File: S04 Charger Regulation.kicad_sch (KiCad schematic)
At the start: 24 parts, among them Q6 DMT4011LFG, Q7 DMT4011LFG, U1 LTC1960

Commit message: Add D5: DNP alternate for D2 at its original 0.5.0 position
- S04: D5 (SS0540, SOD-123) in parallel with D2 on the charger switch
  node and GND, marked DNP, with a NOTE explaining it is an alternate
  to D2.
- PCB: D5 placed where D2 sat on the Altium 0.5.0 board (pads at
  195.70/126.27 and 195.70/129.54, rotated 270). The Net-(D2-C) F.Cu
  pour gets a small tab to reach the D5 cathode; the anode is in the
  GND pour. Zones refilled.
- The board diff is mostly KiCad re-sorting the FET paste-window pads
  on save; no other geometry changed.

ERC 0. DRC: 0 unconnected, 0 parity; remaining items unchanged
(excluded layer-marker edge clearances, silk overlap, text thickness).

Co-Authored-By: Claude Opus 5.5 <noreply@anthropic.com>
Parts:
- added D5: SS0540 40V, EVO2513-0_5_0-import-fps:Diode SOD123, symbol Lattech Systems:Diode Schottky SS0540 0.5A SOD-123
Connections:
- net GND: now also D5.2 (A)
- net at C16.2, D2.1 (C), L1.1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: now also D5.1 (C)

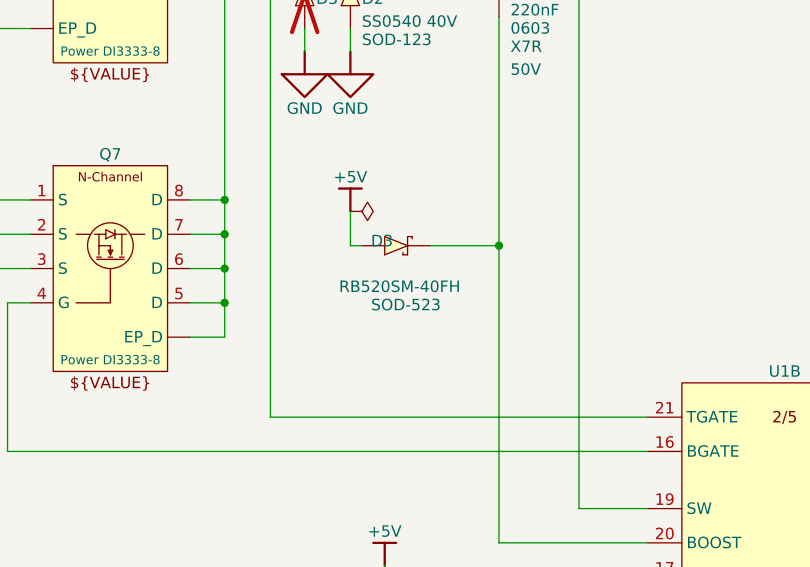
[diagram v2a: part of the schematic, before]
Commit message: D3: KiCad D_SOD-523 footprint, Rohm manufacturer and reel part number
- D3 (RB520SM-40FH) moves from the imported "Diode SOD523" footprint to
  Diode_SMD:D_SOD-523 with the KiCad 3D model; embedded SOD523.STEP dropped.
- MANUFACTURER: On Semiconductor -> Rohm Semiconductor.
- MANUFACTURER_PN: RB520SM-40FH -> RB520SM-40FHT2R (tape and reel).

Co-Authored-By: Claude Opus 5.5 <noreply@anthropic.com>
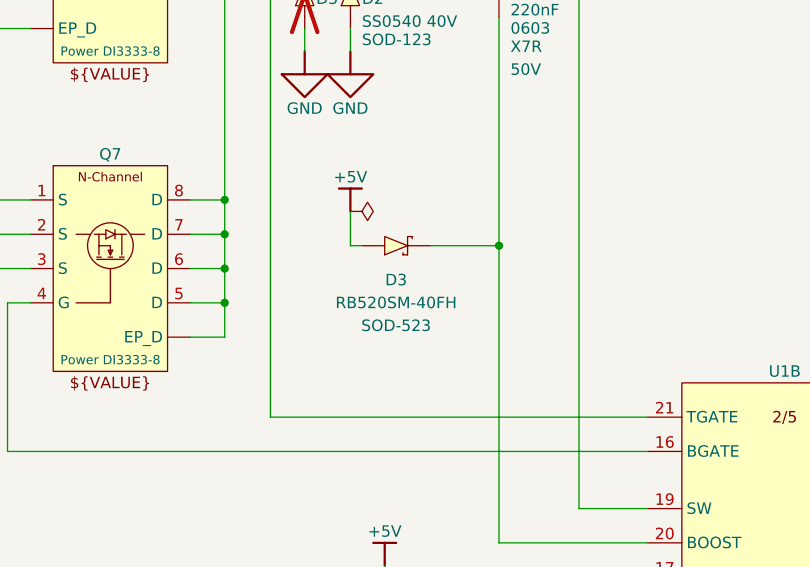
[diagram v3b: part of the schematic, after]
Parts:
- D3: footprint EVO2513-0_5_0-import-fps:Diode SOD523 -> Diode_SMD:D_SOD-523; MANUFACTURER On Semiconductor -> Rohm Semiconductor; MANUFACTURER_PN RB520SM-40FH -> RB520SM-40FHT2R
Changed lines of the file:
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@@
 		(in_pos_files yes)
 		(dnp no)
+		(fields_autoplaced yes)
 		(property "Reference" "D3"
-			(at 145.796 125.73 0)
+			(at 148.59 130.81 0)
 			(show_name no)
 			(do_not_autoplace no)
@@
 					(size 1.27 1.27)
 				)
-				(justify left bottom)
 			)
 		)
@@
 			)
 		)
-		(property "Footprint" "EVO2513-0_5_0-import-fps:Diode SOD523"
+		(property "Footprint" "Diode_SMD:D_SOD-523"
 			(at 148.59 127 0)
 			(hide yes)
@@
 			)
 		)
-		(property "MANUFACTURER" "On Semiconductor"
+		(property "MANUFACTURER" "Rohm Semiconductor"
 			(at 144.272 125.73 0)
 			(hide yes)
@@
 			)
 		)
-		(property "MANUFACTURER_PN" "RB520SM-40FH"
+		(property "MANUFACTURER_PN" "RB520SM-40FHT2R"
 			(at 144.272 125.73 0)
 			(hide yes)
@@
 		)
 		(property "ALTIUM_VALUE" "RB520SM-40FH"
-			(at 142.24 130.81 0)
+			(at 148.59 133.35 0)
 			(show_name no)
 			(do_not_autoplace no)
@@
 					(size 1.27 1.27)
 				)
-				(justify left bottom)
 			)
 		)
 		(property "ALTIUM_FOOTPRINT" "SOD-523"
-			(at 145.796 132.842 0)
+			(at 148.59 135.89 0)
 			(show_name no)
 			(do_not_autoplace no)
@@
 					(size 1.27 1.27)
 				)
-				(justify left bottom)
 			)
 		)

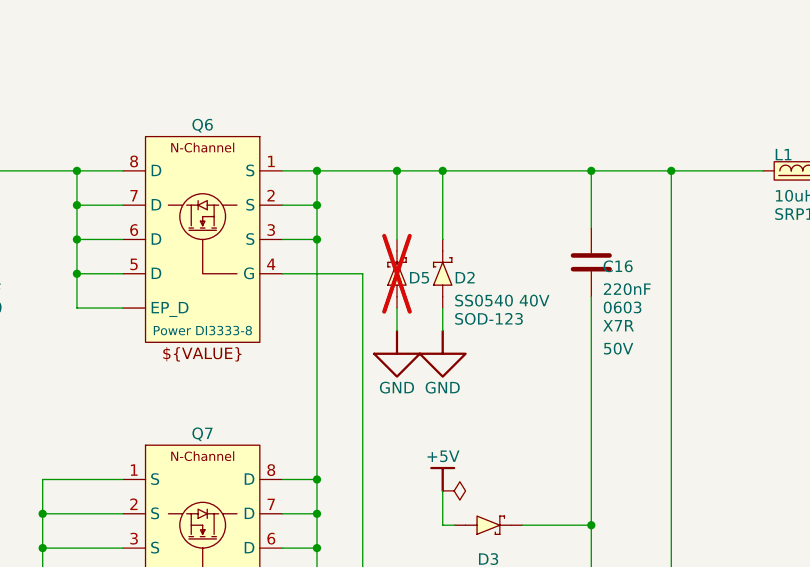
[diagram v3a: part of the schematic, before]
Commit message: Remove D5, the DNP alternate for D2
D2's position and the SW routing are settled, so the optional D5 is
dropped from the schematic, the board and the README. Its GND symbol,
stub wires and junction go with it.

Co-Authored-By: Claude Opus 5.5 <noreply@anthropic.com>
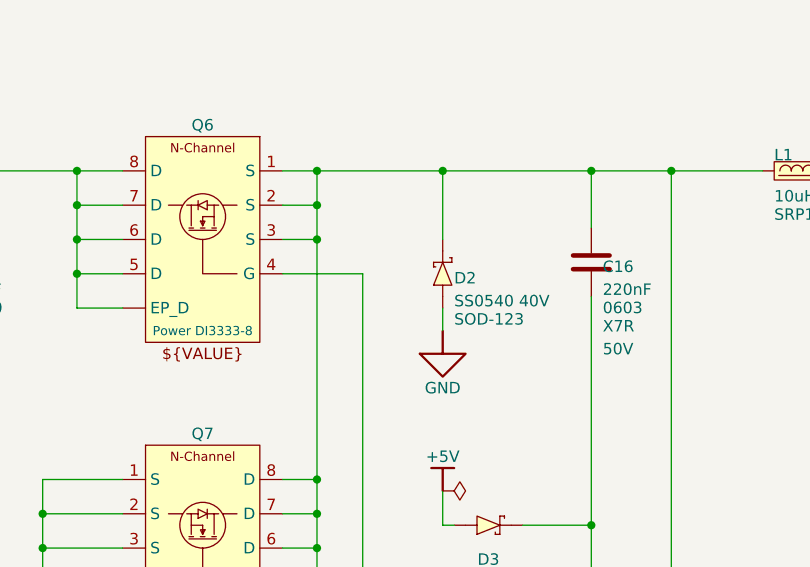
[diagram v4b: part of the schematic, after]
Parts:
- removed D5: SS0540 40V, EVO2513-0_5_0-import-fps:Diode SOD123, symbol Lattech Systems:Diode Schottky SS0540 0.5A SOD-123

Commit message: D2: KiCad D_SOD-123 footprint
D2 (Panjit SS0540) moves from the imported "Diode SOD123" footprint to
Diode_SMD:D_SOD-123 with the KiCad 3D model; pads are within 0.07 mm of
Panjit's land pattern. Embedded STEP dropped from the footprint.

Co-Authored-By: Claude Opus 5.5 <noreply@anthropic.com>
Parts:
- D2: footprint EVO2513-0_5_0-import-fps:Diode SOD123 -> Diode_SMD:D_SOD-123
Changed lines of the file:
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@@
 			)
 		)
-		(property "Footprint" "EVO2513-0_5_0-import-fps:Diode SOD123"
+		(property "Footprint" "Diode_SMD:D_SOD-123"
 			(at 143.51 99.06 0)
 			(hide yes)

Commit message: Fill manufacturer part numbers from the 0.5.0 build orders
Set MANUFACTURER and MANUFACTURER_PN on every fitted part, in the
schematic and on the board. Unchanged parts take the exact part numbers
ordered for the 0.5.0 backup build (DigiKey list and Mouser basket);
changed parts reuse an ordered part where value, package and rating
match; the rest keep the schematic's part or take a Yageo RC/CC part.

Co-Authored-By: Claude Opus 5.5 <noreply@anthropic.com>
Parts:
- C13, C14, C24, C25, C26: MANUFACTURER Murata -> Murata Electronics
- C15: MANUFACTURER (none) -> Murata Electronics; MANUFACTURER_PN (none) -> GRM219R61A475KE34J
- C16, C22: MANUFACTURER Yageo -> YAGEO; MANUFACTURER_PN CC0603KRX7R9BB224 -> AC0603KRX7R9BB224
- C17, C18, C20, C21: MANUFACTURER Yageo -> YAGEO
- C19: MANUFACTURER ? -> YAGEO; MANUFACTURER_PN ? -> CC0402JRNPO9BN101
- C23: MANUFACTURER ? -> Samsung Electro-Mechanics; MANUFACTURER_PN ? -> CL10A105KB8NNNC
- D2: MANUFACTURER Panjit -> Panjit International Inc.; MANUFACTURER_PN SS0540 -> SS0540_R1_00001
- L1: MANUFACTURER Bourns -> Bourns Inc.
- Q6, Q7: MANUFACTURER Diodes Inc -> Diodes Incorporated; MANUFACTURER_PN DMT4011LFG -> DMT4011LFG-13
- R19: MANUFACTURER (none) -> Bourns Inc.
- R20: MANUFACTURER (none) -> YAGEO; MANUFACTURER_PN (none) -> RC0402FR-073K6L
- R21: MANUFACTURER ? -> YAGEO; MANUFACTURER_PN ? -> RC0402FR-07100RL
- U1: MANUFACTURER Analog Devices -> Analog Devices Inc.; MANUFACTURER_PN LTC1960CUHF -> LTC1960CUHF#PBF
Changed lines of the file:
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@@
 			)
 		)
-		(property "MANUFACTURER" "?"
+		(property "MANUFACTURER" "YAGEO"
 			(at 220.98 176.022 0)
 			(hide yes)
@@
 			)
 		)
-		(property "MANUFACTURER_PN" "?"
+		(property "MANUFACTURER_PN" "CC0402JRNPO9BN101"
 			(at 220.98 176.022 0)
 			(hide yes)
@@
 			)
 		)
-		(property "MANUFACTURER" "?"
+		(property "MANUFACTURER" "YAGEO"
 			(at 246.634 127.762 0)
 			(hide yes)
@@
 			)
 		)
-		(property "MANUFACTURER_PN" "?"
+		(property "MANUFACTURER_PN" "RC0402FR-07100RL"
 			(at 246.634 127.762 0)
 			(hide yes)
@@
 			)
 		)
-		(property "MANUFACTURER" ""
+		(property "MANUFACTURER" "Murata Electronics"
 			(at 148.59 168.402 0)
 			(hide yes)
@@
 			)
 		)
-		(property "MANUFACTURER_PN" ""
+		(property "MANUFACTURER_PN" "GRM219R61A475KE34J"
 			(at 148.59 168.402 0)
 			(hide yes)
@@
 			)
 		)
-		(property "MANUFACTURER" "Diodes Inc"
+		(property "MANUFACTURER" "Diodes Incorporated"
 			(at 125.222 81.28 0)
 			(hide yes)
@@
 			)
 		)
-		(property "MANUFACTURER_PN" "DMT4011LFG"
+		(property "MANUFACTURER_PN" "DMT4011LFG-13"
 			(at 125.222 81.28 0)
 			(hide yes)
@@
 			)
 		)
-		(property "MANUFACTURER" "Bourns"
+		(property "MANUFACTURER" "Bourns Inc."
 			(at 178.562 86.614 0)
 			(hide yes)
@@
 			)
 		)
-		(property "MANUFACTURER" "Murata"
+		(property "MANUFACTURER" "Murata Electronics"
 			(at 295.91 94.742 0)
 			(hide yes)
@@
 			)
 		)
-		(property "MANUFACTURER" "Murata"
+		(property "MANUFACTURER" "Murata Electronics"
 			(at 76.2 93.472 0)
 			(hide yes)
@@
 			)
 		)
-		(property "MANUFACTURER" "?"
+		(property "MANUFACTURER" "Samsung Electro-Mechanics"
 			(at 269.24 94.742 0)
 			(hide yes)
@@
 			)
 		)
-		(property "MANUFACTURER_PN" "?"
+		(property "MANUFACTURER_PN" "CL10A105KB8NNNC"
 			(at 269.24 94.742 0)
 			(hide yes)
@@
 			)
 		)
-		(property "MANUFACTURER" "Yageo"
+		(property "MANUFACTURER" "YAGEO"
 			(at 246.38 140.462 0)
 			(hide yes)
@@
 			)
 		)
-		(property "MANUFACTURER" "Diodes Inc"
+		(property "MANUFACTURER" "Diodes Incorporated"
 			(at 107.442 115.57 0)
 			(hide yes)
@@
 			)
 		)
-		(property "MANUFACTURER_PN" "DMT4011LFG"
+		(property "MANUFACTURER_PN" "DMT4011LFG-13"
 			(at 107.442 115.57 0)
 			(hide yes)
@@
 			)
 		)
-		(property "MANUFACTURER" "Murata"
+		(property "MANUFACTURER" "Murata Electronics"
 			(at 283.21 94.742 0)
 			(hide yes)
@@
 			)
 		)
-		(property "MANUFACTURER" ""
+		(property "MANUFACTURER" "YAGEO"
 			(at 231.394 165.862 0)
 			(hide yes)
@@
 			)
 		)
-		(property "MANUFACTURER_PN" ""
+		(property "MANUFACTURER_PN" "RC0402FR-073K6L"
 			(at 231.394 165.862 0)
 			(hide yes)
@@
 			)
 		)
-		(property "MANUFACTURER" "Analog Devices"
+		(property "MANUFACTURER" "Analog Devices Inc."
 			(at 176.022 142.24 0)
 			(hide yes)
@@
 			)
 		)
-		(property "MANUFACTURER_PN" "LTC1960CUHF"
+		(property "MANUFACTURER_PN" "LTC1960CUHF#PBF"
 			(at 176.022 142.24 0)
 			(hide yes)
@@
 			)
 		)
-		(property "MANUFACTURER" ""
+		(property "MANUFACTURER" "Bourns Inc."
 			(at 225.552 83.82 90)
 			(hide yes)
@@
 			)
 		)
-		(property "MANUFACTURER" "Murata"
+		(property "MANUFACTURER" "Murata Electronics"
 			(at 308.61 94.742 0)
 			(hide yes)
@@
 			)
 		)
-		(property "MANUFACTURER" "Yageo"
+		(property "MANUFACTURER" "YAGEO"
 			(at 246.38 176.022 0)
 			(hide yes)
@@
 			)
 		)
-		(property "MANUFACTURER_PN" "CC0603KRX7R9BB224"
+		(property "MANUFACTURER_PN" "AC0603KRX7R9BB224"
 			(at 246.38 176.022 0)
 			(hide yes)
@@
 			)
 		)
-		(property "MANUFACTURER" "Yageo"
+		(property "MANUFACTURER" "YAGEO"
 			(at 158.75 168.402 0)
 			(hide yes)
@@
 			)
 		)
-		(property "MANUFACTURER" "Panjit"
+		(property "MANUFACTURER" "Panjit International Inc."
 			(at 142.24 94.742 90)
 			(hide yes)
@@
 			)
 		)
-		(property "MANUFACTURER_PN" "SS0540"
+		(property "MANUFACTURER_PN" "SS0540_R1_00001"
 			(at 142.24 94.742 90)
 			(hide yes)
@@
 			)
 		)
-		(property "MANUFACTURER" "Yageo"
+		(property "MANUFACTURER" "YAGEO"
 			(at 158.75 93.472 0)
 			(hide yes)
@@
 			)
 		)
-		(property "MANUFACTURER_PN" "CC0603KRX7R9BB224"
+		(property "MANUFACTURER_PN" "AC0603KRX7R9BB224"
 			(at 158.75 93.472 0)
 			(hide yes)
@@
 			)
 		)
-		(property "MANUFACTURER" "Murata"
+		(property "MANUFACTURER" "Murata Electronics"
 			(at 87.63 93.472 0)
 			(hide yes)
@@
 			)
 		)
-		(property "MANUFACTURER" "Yageo"
+		(property "MANUFACTURER" "YAGEO"
 			(at 231.14 176.022 0)
 			(hide yes)
@@
 			)
 		)
-		(property "MANUFACTURER" "Yageo"
+		(property "MANUFACTURER" "YAGEO"
 			(at 210.82 176.022 0)
 			(hide yes)

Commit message: Move capacitors to currently available part numbers
C32 to Murata GRM219R61C226ME15L (GRM21BR61C226ME44L is no longer
generally available), C39 to Yageo CC0805KPX7R9BB102, the 1 uF 0603
caps to Murata GRT188R61H105KE13D, and the 10 uF 1210 caps to Taiyo
Yuden UMK325AB7106KMHP.

Co-Authored-By: Claude Opus 5.5 <noreply@anthropic.com>
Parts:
- C13, C14, C24, C25, C26: MANUFACTURER Murata Electronics -> Taiyo Yuden; MANUFACTURER_PN GRM32ER71H106KA12L -> UMK325AB7106KMHP
- C23: MANUFACTURER Samsung Electro-Mechanics -> Murata Electronics; MANUFACTURER_PN CL10A105KB8NNNC -> GRT188R61H105KE13D
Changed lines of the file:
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@@
 			)
 		)
-		(property "MANUFACTURER" "Murata Electronics"
+		(property "MANUFACTURER" "Taiyo Yuden"
 			(at 295.91 94.742 0)
 			(hide yes)
@@
 			)
 		)
-		(property "MANUFACTURER_PN" "GRM32ER71H106KA12L"
+		(property "MANUFACTURER_PN" "UMK325AB7106KMHP"
 			(at 295.91 94.742 0)
 			(hide yes)
@@
 			)
 		)
-		(property "MANUFACTURER" "Murata Electronics"
+		(property "MANUFACTURER" "Taiyo Yuden"
 			(at 76.2 93.472 0)
 			(hide yes)
@@
 			)
 		)
-		(property "MANUFACTURER_PN" "GRM32ER71H106KA12L"
+		(property "MANUFACTURER_PN" "UMK325AB7106KMHP"
 			(at 76.2 93.472 0)
 			(hide yes)
@@
 			)
 		)
-		(property "MANUFACTURER" "Samsung Electro-Mechanics"
+		(property "MANUFACTURER" "Murata Electronics"
 			(at 269.24 94.742 0)
 			(hide yes)
@@
 			)
 		)
-		(property "MANUFACTURER_PN" "CL10A105KB8NNNC"
+		(property "MANUFACTURER_PN" "GRT188R61H105KE13D"
 			(at 269.24 94.742 0)
 			(hide yes)
@@
 			)
 		)
-		(property "MANUFACTURER" "Murata Electronics"
+		(property "MANUFACTURER" "Taiyo Yuden"
 			(at 283.21 94.742 0)
 			(hide yes)
@@
 			)
 		)
-		(property "MANUFACTURER_PN" "GRM32ER71H106KA12L"
+		(property "MANUFACTURER_PN" "UMK325AB7106KMHP"
 			(at 283.21 94.742 0)
 			(hide yes)
@@
 			)
 		)
-		(property "MANUFACTURER" "Murata Electronics"
+		(property "MANUFACTURER" "Taiyo Yuden"
 			(at 308.61 94.742 0)
 			(hide yes)
@@
 			)
 		)
-		(property "MANUFACTURER_PN" "GRM32ER71H106KA12L"
+		(property "MANUFACTURER_PN" "UMK325AB7106KMHP"
 			(at 308.61 94.742 0)
 			(hide yes)
@@
 			)
 		)
-		(property "MANUFACTURER" "Murata Electronics"
+		(property "MANUFACTURER" "Taiyo Yuden"
 			(at 87.63 93.472 0)
 			(hide yes)
@@
 			)
 		)
-		(property "MANUFACTURER_PN" "GRM32ER71H106KA12L"
+		(property "MANUFACTURER_PN" "UMK325AB7106KMHP"
 			(at 87.63 93.472 0)
 			(hide yes)
